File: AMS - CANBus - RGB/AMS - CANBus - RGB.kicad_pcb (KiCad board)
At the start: 2 copper layers, 72.9 x 71.1 mm, 45 parts, among them IC2 OPA4340UA, J1 Power_And_CAN, J2 Power_And_CAN, J3 TTL_Programmer, J4 ICSP, J5 Conn_01x02, J6 Screw_Terminal_01x02, Q1 IRF9Z34NPBF, U1 3568, U2 ATmega328P-P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

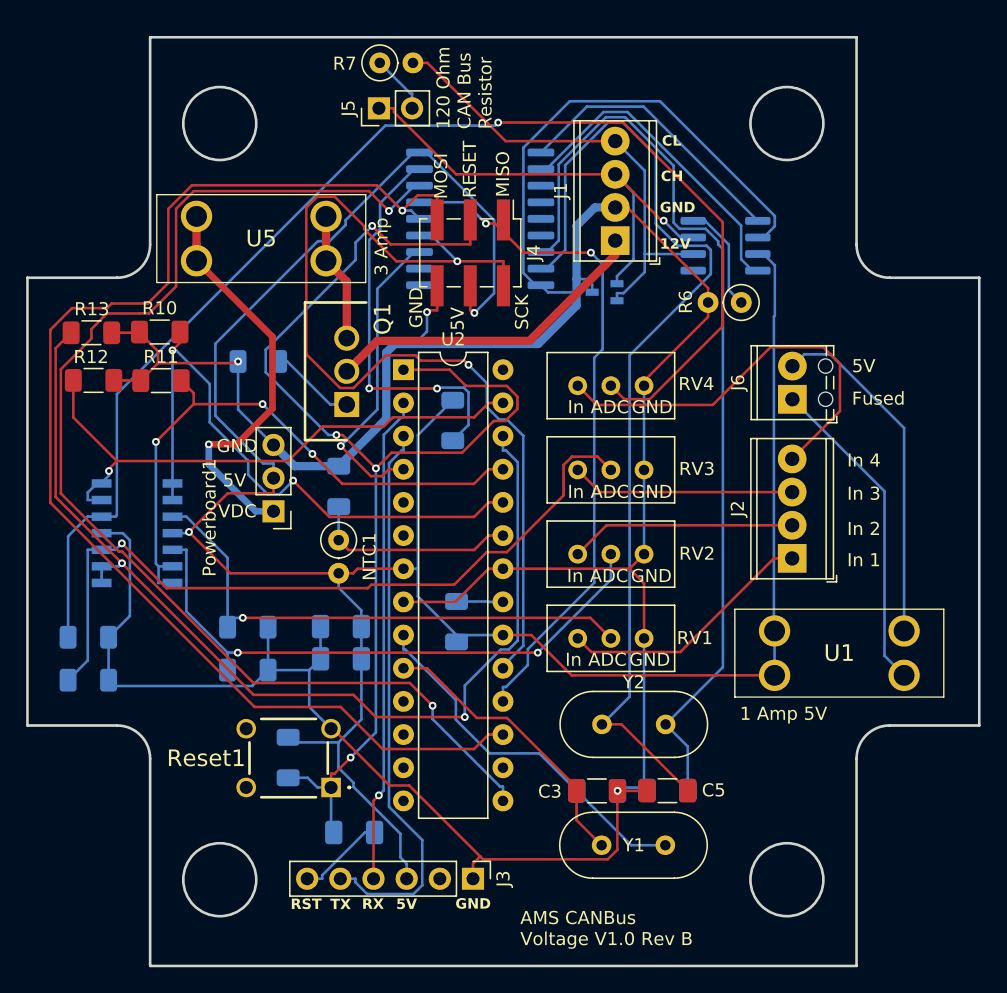
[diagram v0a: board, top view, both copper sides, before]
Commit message: removal of the Input stuff from the Voltage Board this was copied from
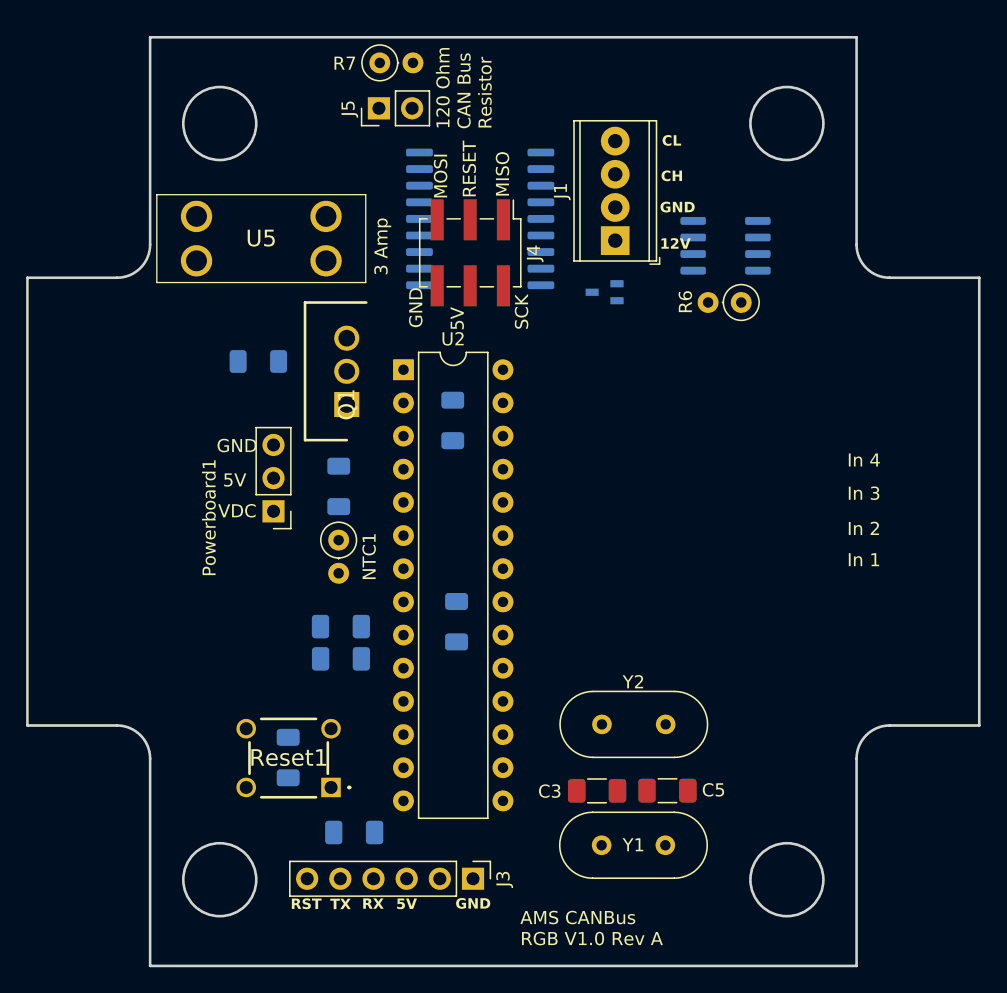
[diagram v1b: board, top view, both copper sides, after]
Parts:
- removed IC2: OPA4340UA, SamacSys_Parts:SOIC127P600X175-14N
- removed J2: Power_And_CAN, TerminalBlock_Phoenix:TerminalBlock_Phoenix_MPT-0,5-4-2.54_1x04_P2.54mm_Horizontal
- removed J6: Screw_Terminal_01x02, TerminalBlock_Phoenix:TerminalBlock_Phoenix_MPT-0,5-2-2.54_1x02_P2.54mm_Horizontal
- removed R10, R11, R12, R13: 47K, Resistor_SMD:R_1206_3216Metric_Pad1.30x1.75mm_HandSolder
- removed R14, R15, R8, R9: 100K, Resistor_SMD:R_1206_3216Metric_Pad1.30x1.75mm_HandSolder
- removed RV1, RV2, RV3, RV4: 200k, Potentiometer_THT:Potentiometer_Bourns_3296W_Vertical
- removed U1: 3568, SamacSys_Parts:3568
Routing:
- net GND: track 258.1 -> 0.00 mm, vias 3 -> 0
- net +5V: track 189.5 -> 0.00 mm, vias 2 -> 0
- net /BareMinAtmel328P/PB3-D11-MOSI: track 98.5 -> 0.00 mm, vias 1 -> 0
- net /BufferedADC/ADCIN4: track 98.3 -> 0.00 mm, vias 1 -> 0
- net /BareMinAtmel328P/PB1-D9: track 92.4 -> 0.00 mm, vias 2 -> 0
- net /BareMinAtmel328P/RESET: track 92.1 -> 0.00 mm, vias 4 -> 0
- net /BareMinAtmel328P/PC3-A3: track 78.5 -> 0.00 mm, vias 2 -> 0
- net Net-(U3-OSC1): track 76.6 -> 0.00 mm
- net /BareMinAtmel328P/PB5-D13-SCK: track 74.2 -> 0.00 mm, vias 2 -> 0
- net Net-(U3-OSC2): track 72.0 -> 0.00 mm
- net /BufferedADC/ADCIN3: track 57.7 -> 0.00 mm, vias 1 -> 0
- net /BareMinAtmel328P/PB4-D12-MISO: track 52.8 -> 0.00 mm, vias 2 -> 0
- net /BareMinAtmel328P/PC1-A1: track 47.4 -> 0.00 mm, vias 2 -> 0
- net /BareMinAtmel328P/PC2-A2: track 46.0 -> 0.00 mm, vias 3 -> 0
- net /BufferedADC/ADCIN2: track 45.2 -> 0.00 mm, vias 2 -> 0
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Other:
- board text added: "AMS CANBus RGB V1.0 Rev A"
- board text removed: "1 Amp 5V"
- board text removed: "ADC"
- board text removed: "AMS CANBus Voltage V1.0 Rev B"
- board text removed: "Fused"
- board text removed: "In"
